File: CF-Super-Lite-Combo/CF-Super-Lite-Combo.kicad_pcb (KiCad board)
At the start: 2 copper layers, 99.9 x 99.9 mm, 21 parts, among them J1 IDE_CONNECTOR, J2 CF Adapter Power, J3 Jumpers, J4 Bus_ISA_8bit, U1 BIOS FLASH, U2 74HCT245, U3 GAL22V10, U4 DS1315, U5 AS6C4008-55PCN, Y1 32.768 KHz

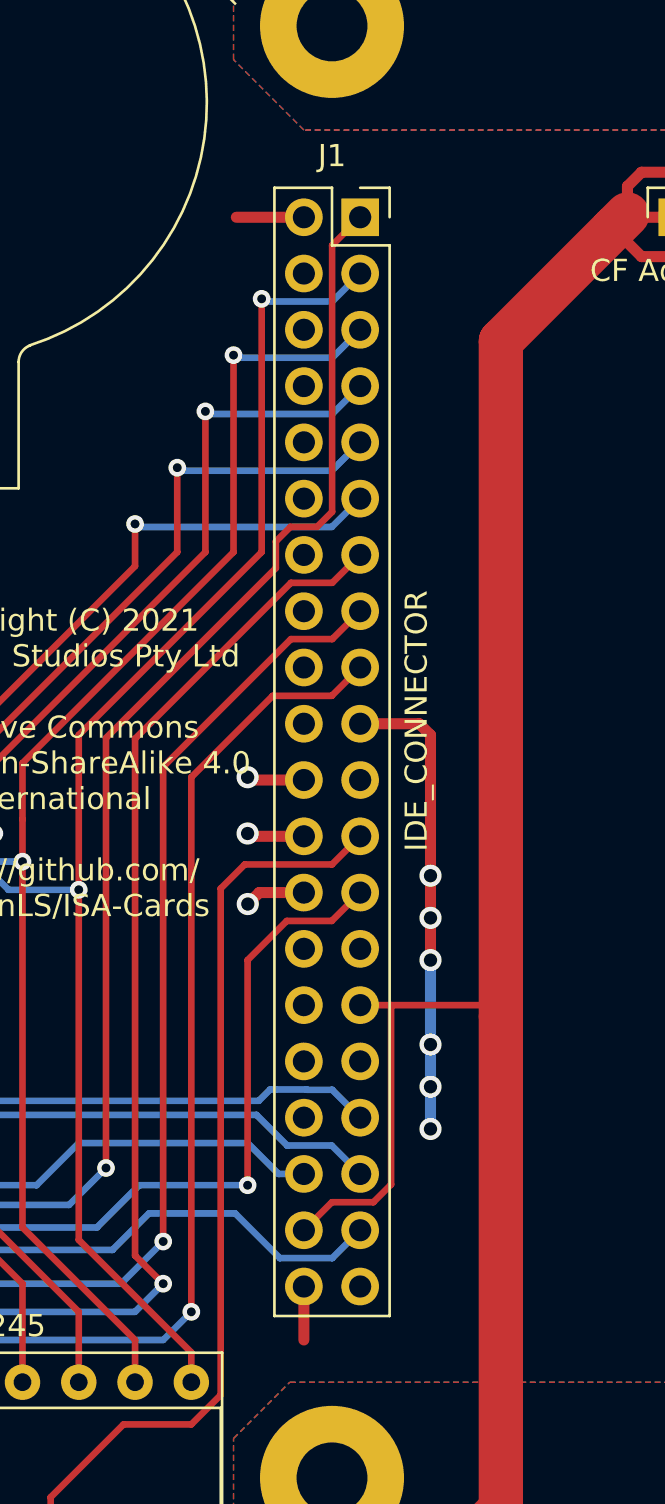
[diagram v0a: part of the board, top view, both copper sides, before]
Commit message: CF-Super-Lite-Combo: Rotate CF adapter header 180 degrees. Routing still needs to be corrected.
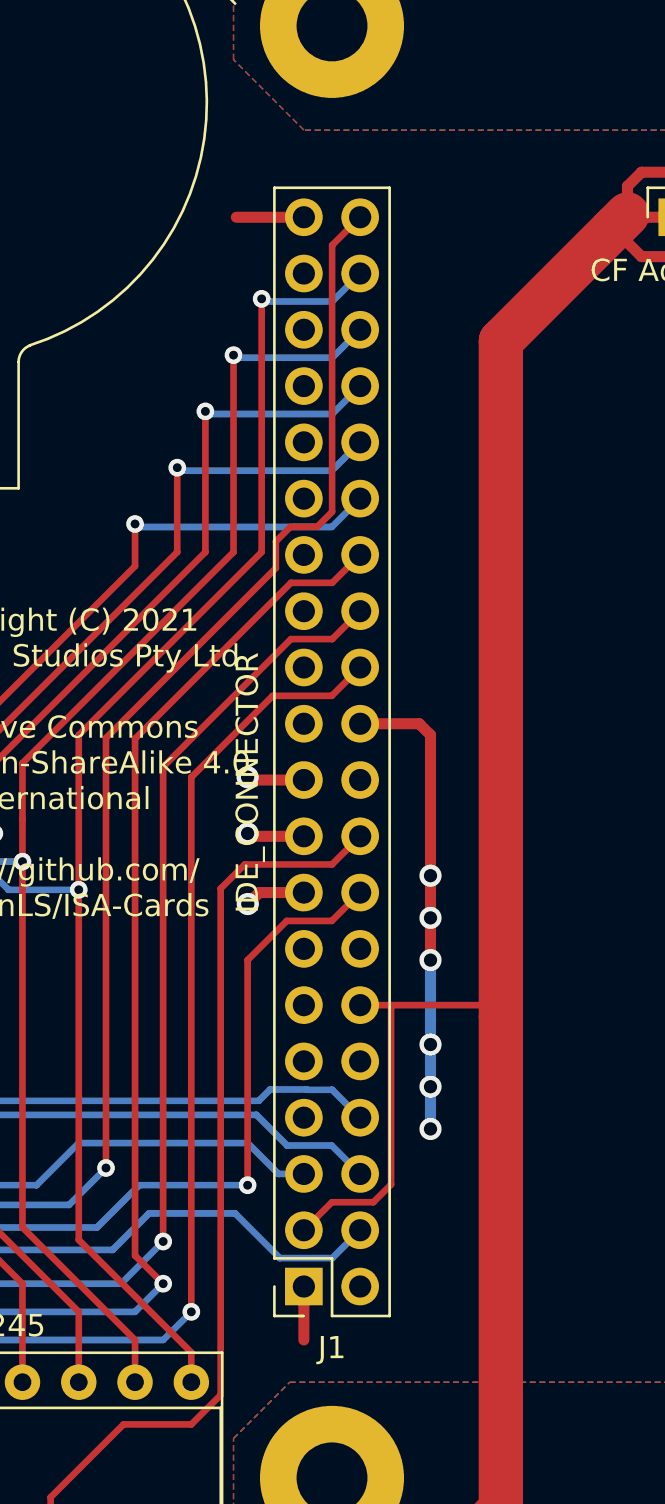
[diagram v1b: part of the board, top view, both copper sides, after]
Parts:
- moved J1 48.3 mm to (165.1, 108.1), turned to 180 degrees
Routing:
- net GND: track 230.4 -> 219.6 mm, vias 38 -> 36
- net Net-(J1-Pad39): track 0.00 -> 3.05 mm
- net D1_BUF: track 82.8 -> 85.5 mm, vias 2 -> 3
- net D0_BUF: track 109.5 -> 112.1 mm, vias 1 -> 2
- net ~RESET: track 100.5 -> 102.9 mm

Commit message: CF-Super-Lite-Combo: Finished pass at fixing layout. Ready for production.
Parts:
- removed the J3 at (101.6, 61.0)
- added J4: Addresses, Connector_PinHeader_2.54mm:PinHeader_2x03_P2.54mm_Vertical, F.Cu at (101.6, 55.9)
- added J5: Addresses, Connector_PinHeader_2.54mm:PinHeader_2x03_P2.54mm_Vertical, F.Cu at (108.0, 55.9)
- J2: footprint Connector_PinSocket_2.54mm:PinSocket_1x01_P2.54mm_Vertical -> Connector_PinSocket_2.54mm:PinSocket_1x02_P2.54mm_Vertical
- moved Y1 0.64 mm to (120.0, 52.7)
- moved C4 0.63 mm to (114.3, 55.9)
- moved U4 0.63 mm to (117.5, 63.5)
- turned J2 to 270 degrees
- renumbered J4 to J3
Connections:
- U1 pad 29: ATA_ADDR_JUMPER -> A14
- U1 pad 3: V20_JUMPER -> ATA_ADDR_JUMPER
- U3 pad 22: ROM_ADDR_JUMPER -> ATA_ADDR_JUMPER
- U3 pad 23: ATA_ADDR_JUMPER -> ROM_ADDR_JUMPER
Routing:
- net GND: track 219.6 -> 344.5 mm, vias 36 -> 64
- net VCC: track 560.1 -> 454.5 mm
- net ~RESET: track 102.9 -> 56.2 mm, vias 2 -> 1
- net ~CS1~_ATA: track 59.9 -> 96.9 mm, vias 1 -> 2
- net A14: track 63.6 -> 99.4 mm, vias 2 -> 4
- net V20_JUMPER: track 30.9 -> 0.00 mm
- net D2_BUF: track 85.4 -> 58.8 mm, vias 2 -> 1
- net D7_BUF: track 104.0 -> 78.6 mm
- net D0_BUF: track 112.1 -> 88.9 mm, vias 2 -> 0
- net D6_BUF: track 97.6 -> 77.2 mm
- net D5_BUF: track 93.3 -> 75.6 mm
- net D1_BUF: track 85.5 -> 68.8 mm, vias 3 -> 0
- net D4_BUF: track 86.5 -> 72.6 mm
- net D3_BUF: track 81.7 -> 69.8 mm
- net A10: track 111.2 -> 123.0 mm
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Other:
- board text added: "300h"
- board text added: "320h"
- board text added: "6pF"
- board text added: "ABSENT"
- board text added: "C800h"
- board text added: "CF COMBO SUPER-LITE"
- board text added: "Compact Flash with XT-IDE BIOS"
- board text added: "Compact Flash with XT-IDE BIOS and SmartWatch"
- board text added: "Compact Flash with XT-IDE BIOS, SmartWatch and 512K SRAM. For original Tandy 1000, 1000A or 1000 HD only. Remove any other RAM upgrade before installing."
- board text added: "D000h"
- board text added: "In memory of my father, Michael James Lee-Steere. Our early experiences with the Tandy 1000 provided the inspiration for creating this upgrade."
- board text added: "PRESENT"
- board text added: "ROM ADDR"
- board text added: "Thanks to the XTIDE Universal BIOS Team and others who contributed to the XTIDE Universal BIOS. Additional thanks to Rob Krenicki, Jacob Dorne/Monotech PCs and James Pearce/Lo-tech for their influencing works."
- board text added: "UNUSED"
- board text removed: "8086/8088"
- board text removed: "CPU TYPE"
- board text removed: "PORT 1F0h"
- board text removed: "Port 320h"
- board text removed: "ROM ADDR."
- board text removed: "ROM C800h"
- board text removed: "ROM D800h"
- board text removed: "RTC ABSENT"
- board text removed: "RTC PRESENT"
- board text removed: "Tandy 1000 Essentials"
- board text removed: "V20, 286,..."
